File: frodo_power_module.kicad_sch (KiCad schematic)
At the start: 76 parts, among them J1 Keystone 1048, J1 Molex MicroFit 2x3, J10 SWD Header, J2 Molex MicroFit 2x3, J3 Molex MicroFit 2x2, J4 Molex MicroFit 2x2, J5 JST-GH, J6 JST-GH, U1 STM32F042F6Px, U2 L7805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

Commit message: changed connector Bezeichnet due to conflicts and made Keytore 1048 pads little bit bigger
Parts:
- renumbered J1 to J7
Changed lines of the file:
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@@
   (symbol (lib_id "Connector_Generic:Conn_01x06") (at 34.29 124.46 180) (unit 1)
     (in_bom yes) (on_board yes) (dnp no)
-    (property "Reference" "J1" (at 30.48 124.46 0)
+    (property "Reference" "J7" (at 30.48 124.46 0)
       (effects (font (size 1.27 1.27)))
     )
@@
       (project "frodo_power_module"
         (path "/afc8cbd3-9ea8-40a2-afae-ed6bd0fe7e6e"
-          (reference "J1") (unit 1)
+          (reference "J7") (unit 1)
         )
       )

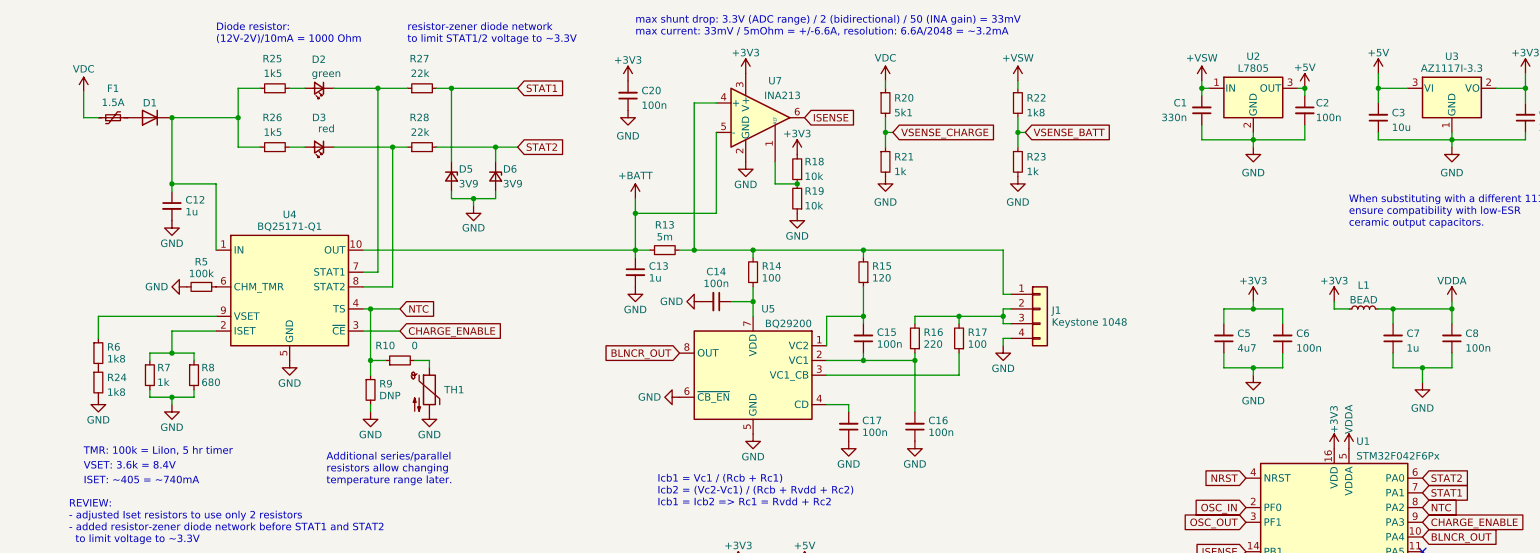
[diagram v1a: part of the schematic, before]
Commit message: added power flags for ERC and removed all errors
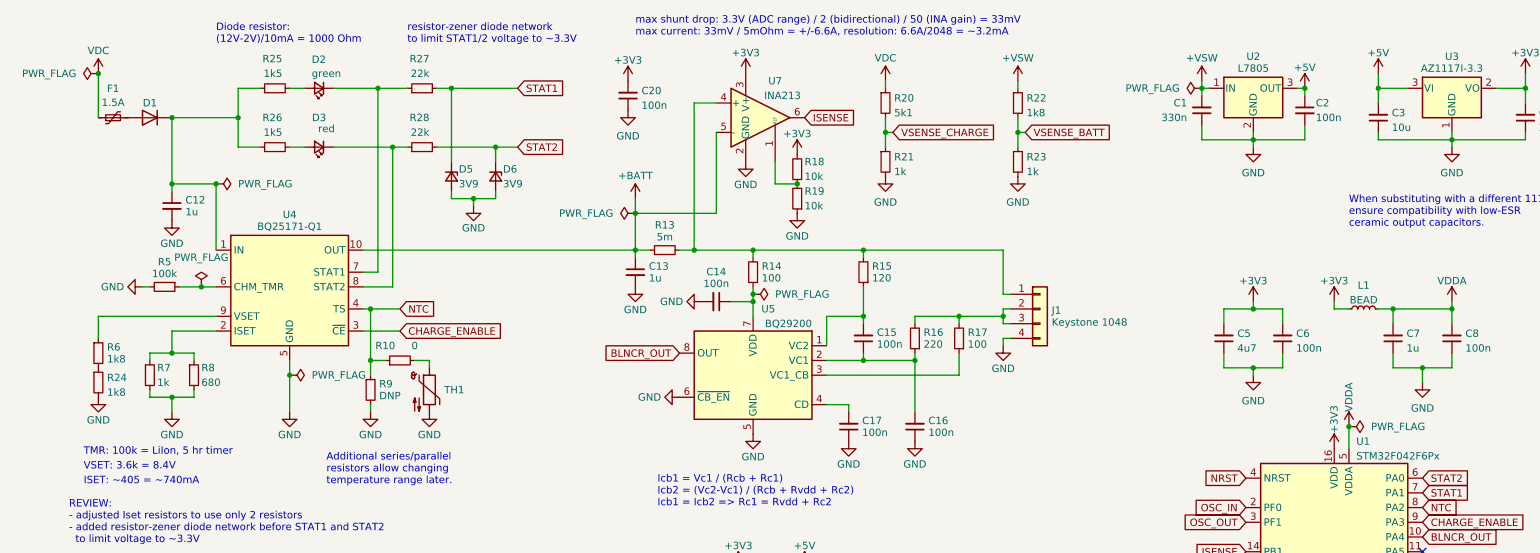
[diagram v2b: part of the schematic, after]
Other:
- moved on the sheet: R5

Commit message: added footprints to D5 D7 J2 and J7. Needs review
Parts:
- D5, D6: footprint (none) -> footprints:SOD323F_DIO-L
- J2, J7: footprint (none) -> Connector_Molex:Molex_Micro-Fit_3.0_43045-0612_2x03_P3.00mm_Vertical
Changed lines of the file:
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@@
       (effects (font (size 1.27 1.27)) (justify left))
     )
-    (property "Footprint" "" (at 90.17 43.18 90)
+    (property "Footprint" "footprints:SOD323F_DIO-L" (at 90.17 43.18 90)
       (effects (font (size 1.27 1.27)) hide)
     )
@@
       (effects (font (size 1.27 1.27)))
     )
-    (property "Footprint" "" (at 34.29 124.46 0)
+    (property "Footprint" "Connector_Molex:Molex_Micro-Fit_3.0_43045-0612_2x03_P3.00mm_Vertical" (at 34.29 124.46 0)
       (effects (font (size 1.27 1.27)) hide)
     )
@@
       (effects (font (size 1.27 1.27)))
     )
-    (property "Footprint" "" (at 34.29 170.18 0)
+    (property "Footprint" "Connector_Molex:Molex_Micro-Fit_3.0_43045-0612_2x03_P3.00mm_Vertical" (at 34.29 170.18 0)
       (effects (font (size 1.27 1.27)) hide)
     )
@@
       (effects (font (size 1.27 1.27)) (justify left))
     )
-    (property "Footprint" "" (at 82.55 43.18 90)
+    (property "Footprint" "footprints:SOD323F_DIO-L" (at 82.55 43.18 90)
       (effects (font (size 1.27 1.27)) hide)
     )

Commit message: worked on pcb
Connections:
- net +3V3: no longer U7.3 (V+)
- net +BATT: no longer U7.5 (-)
- net GND: now also U7.1 (REF); no longer U7.2 (GND)
- net ISENSE: no longer U7.6
- net at R18.1, R19.2: now also U7.2 (GND); no longer U7.1 (REF)
- net at J1.1 (Pin_1), R13.2, R14.2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: no longer U7.4 (+)
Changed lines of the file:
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@@
     )
   )
-  (symbol (lib_id "frodo_power_module:INA210") (at 135.89 33.02 0) (unit 1)
+  (symbol (lib_id "frodo_power_module:INA210") (at 135.89 33.02 0) (mirror y) (unit 1)
     (in_bom yes) (on_board yes) (dnp no)
-    (property "Reference" "U7" (at 138.43 26.67 0)
+    (property "Reference" "U7" (at 133.35 26.67 0)
       (effects (font (size 1.27 1.27)))
     )
-    (property "Value" "INA213" (at 139.7 29.21 0)
+    (property "Value" "INA213" (at 132.08 29.21 0)
       (effects (font (size 1.27 1.27)))
     )
-    (property "Footprint" "Package_TO_SOT_SMD:SOT-363_SC-70-6" (at 137.16 31.75 0)
+    (property "Footprint" "Package_TO_SOT_SMD:SOT-363_SC-70-6" (at 134.62 31.75 0)
       (effects (font (size 1.27 1.27)) hide)
     )
-    (property "Datasheet" "https://www.ti.com/lit/ds/symlink/ina210.pdf" (at 139.7 29.21 0)
+    (property "Datasheet" "https://www.ti.com/lit/ds/symlink/ina210.pdf" (at 132.08 29.21 0)
       (effects (font (size 1.27 1.27)) hide)
     )

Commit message: changed molex footprint from vertical to horiztontal
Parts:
- J2, J7: footprint Connector_Molex:Molex_Micro-Fit_3.0_43045-0612_2x03_P3.00mm_Vertical -> Connector_Molex:Molex_Micro-Fit_3.0_43045-0600_2x03_P3.00mm_Horizontal
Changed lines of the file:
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@@
       (effects (font (size 1.27 1.27)))
     )
-    (property "Footprint" "Connector_Molex:Molex_Micro-Fit_3.0_43045-0612_2x03_P3.00mm_Vertical" (at 34.29 124.46 0)
+    (property "Footprint" "Connector_Molex:Molex_Micro-Fit_3.0_43045-0600_2x03_P3.00mm_Horizontal" (at 34.29 124.46 0)
       (effects (font (size 1.27 1.27)) hide)
     )
@@
       (effects (font (size 1.27 1.27)))
     )
-    (property "Footprint" "Connector_Molex:Molex_Micro-Fit_3.0_43045-0612_2x03_P3.00mm_Vertical" (at 34.29 170.18 0)
-      (effects (font (size 1.27 1.27)) hide)
-    )
+    (property "Footprint" "Connector_Molex:Molex_Micro-Fit_3.0_43045-0600_2x03_P3.00mm_Horizontal" (at 34.29 170.18 0)
+      (effects (font (size 1.27 1.27)) hide)
+    )

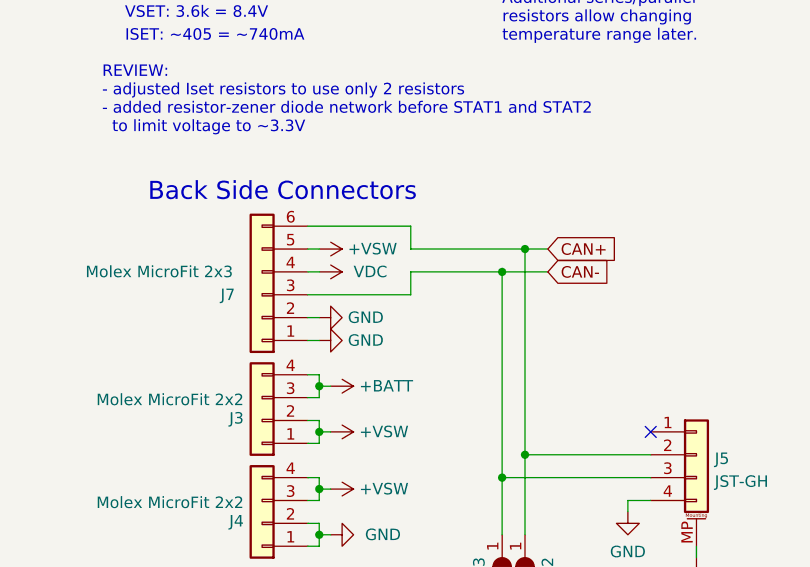
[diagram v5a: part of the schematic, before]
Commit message: Added Power Traces and made CAN+ and CAN- equal size
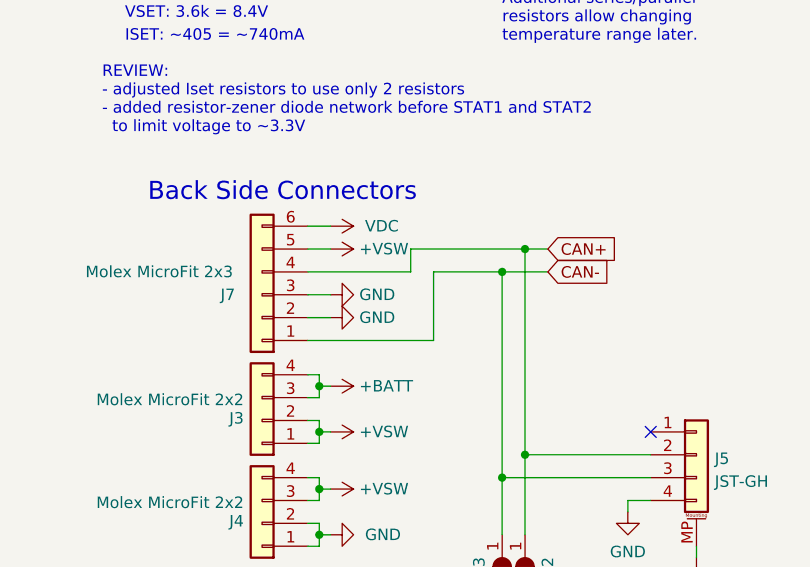
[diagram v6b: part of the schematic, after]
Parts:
- D5, D6: footprint footprints:SOD323F_DIO-L -> Diode_SMD:D_0201_0603Metric
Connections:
- net CAN+: now also J7.4 (Pin_4); no longer J7.6 (Pin_6)
- net CAN-: now also J7.1 (Pin_1); no longer J7.3 (Pin_3)
- net GND: now also J7.3 (Pin_3); no longer J7.1 (Pin_1)
- net VDC: now also J7.6 (Pin_6); no longer J7.4 (Pin_4)

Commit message: worked on file
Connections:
- net +3V3: now also U7.3 (V+)
- net +BATT: now also U7.5 (-)
- net GND: now also U7.2 (GND); no longer U7.1 (REF)
- net ISENSE: now also U7.6
- net at R18.1, R19.2: now also U7.1 (REF); no longer U7.2 (GND)
- net at J1.1 (Pin_1), R13.2, R14.2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: now also U7.4 (+)
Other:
- note added: "Change later S+ to SWDIO and S- to SWCLK"
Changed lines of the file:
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@@
     (effects (font (size 1.27 1.27)) (justify left bottom))
   )
+  (text "Change later S+ to SWDIO and S- to SWCLK\n" (at 195.58 173.99 0)
+    (effects (font (size 5 5)) (justify left bottom))
+  )
   (text "REVIEW:\n- adjusted Iset resistors to use only 2 resistors\n- added resistor-zener diode network before STAT1 and STAT2\n  to limit voltage to ~3.3V"
     (at 16.51 106.68 0)
@@
   (global_label "SWDIO" (shape input) (at 204.47 147.32 180) (fields_autoplaced)
     (effects (font (size 1.27 1.27)) (justify right))
-    (property "Intersheetrefs" "${INTERSHEET_REFS}" (at 196.1907 147.3994 0)
+    (property "Intersheetrefs" "${INTERSHEET_REFS}" (at 195.698 147.32 0)
       (effects (font (size 1.27 1.27)) (justify right) hide)
     )
@@
   (global_label "SWCLK" (shape input) (at 250.19 123.19 0) (fields_autoplaced)
     (effects (font (size 1.27 1.27)) (justify left))
-    (property "Intersheetrefs" "${INTERSHEET_REFS}" (at 258.8321 123.2694 0)
+    (property "Intersheetrefs" "${INTERSHEET_REFS}" (at 259.3248 123.19 0)
       (effects (font (size 1.27 1.27)) (justify left) hide)
     )
@@
   (global_label "SWCLK" (shape input) (at 204.47 149.86 180) (fields_autoplaced)
     (effects (font (size 1.27 1.27)) (justify right))
-    (property "Intersheetrefs" "${INTERSHEET_REFS}" (at 195.8279 149.9394 0)
+    (property "Intersheetrefs" "${INTERSHEET_REFS}" (at 195.3352 149.86 0)
       (effects (font (size 1.27 1.27)) (justify right) hide)
     )
@@
   (global_label "SWDIO" (shape input) (at 250.19 120.65 0) (fields_autoplaced)
     (effects (font (size 1.27 1.27)) (justify left))
-    (property "Intersheetrefs" "${INTERSHEET_REFS}" (at 258.4693 120.7294 0)
+    (property "Intersheetrefs" "${INTERSHEET_REFS}" (at 258.962 120.65 0)
       (effects (font (size 1.27 1.27)) (justify left) hide)
     )
@@
     )
   )
-  (symbol (lib_id "frodo_power_module:INA210") (at 135.89 33.02 0) (mirror y) (unit 1)
+  (symbol (lib_id "frodo_power_module:INA210") (at 135.89 33.02 0) (unit 1)
     (in_bom yes) (on_board yes) (dnp no)
-    (property "Reference" "U7" (at 133.35 26.67 0)
+    (property "Reference" "U7" (at 138.43 26.67 0)
       (effects (font (size 1.27 1.27)))
     )
-    (property "Value" "INA213" (at 132.08 29.21 0)
+    (property "Value" "INA213" (at 139.7 29.21 0)
       (effects (font (size 1.27 1.27)))
     )
-    (property "Footprint" "Package_TO_SOT_SMD:SOT-363_SC-70-6" (at 134.62 31.75 0)
+    (property "Footprint" "Package_TO_SOT_SMD:SOT-363_SC-70-6" (at 137.16 31.75 0)
       (effects (font (size 1.27 1.27)) hide)
     )
-    (property "Datasheet" "https://www.ti.com/lit/ds/symlink/ina210.pdf" (at 132.08 29.21 0)
+    (property "Datasheet" "https://www.ti.com/lit/ds/symlink/ina210.pdf" (at 139.7 29.21 0)
       (effects (font (size 1.27 1.27)) hide)
     )
